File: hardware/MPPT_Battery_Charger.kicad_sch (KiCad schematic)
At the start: 76 parts, among them Q24 SI7414DN-T1-E3, Q25 SI7414DN-T1-E3, Q5 SI7414DN-T1-E3, Q6 SI7414DN-T1-E3, Q8 SI2302DDS-T1-GE3, U22 BQ24650RVAT, U26 LMV321RIYLT, U28 LMV321RIYLT, U4 INA199C1DCKR

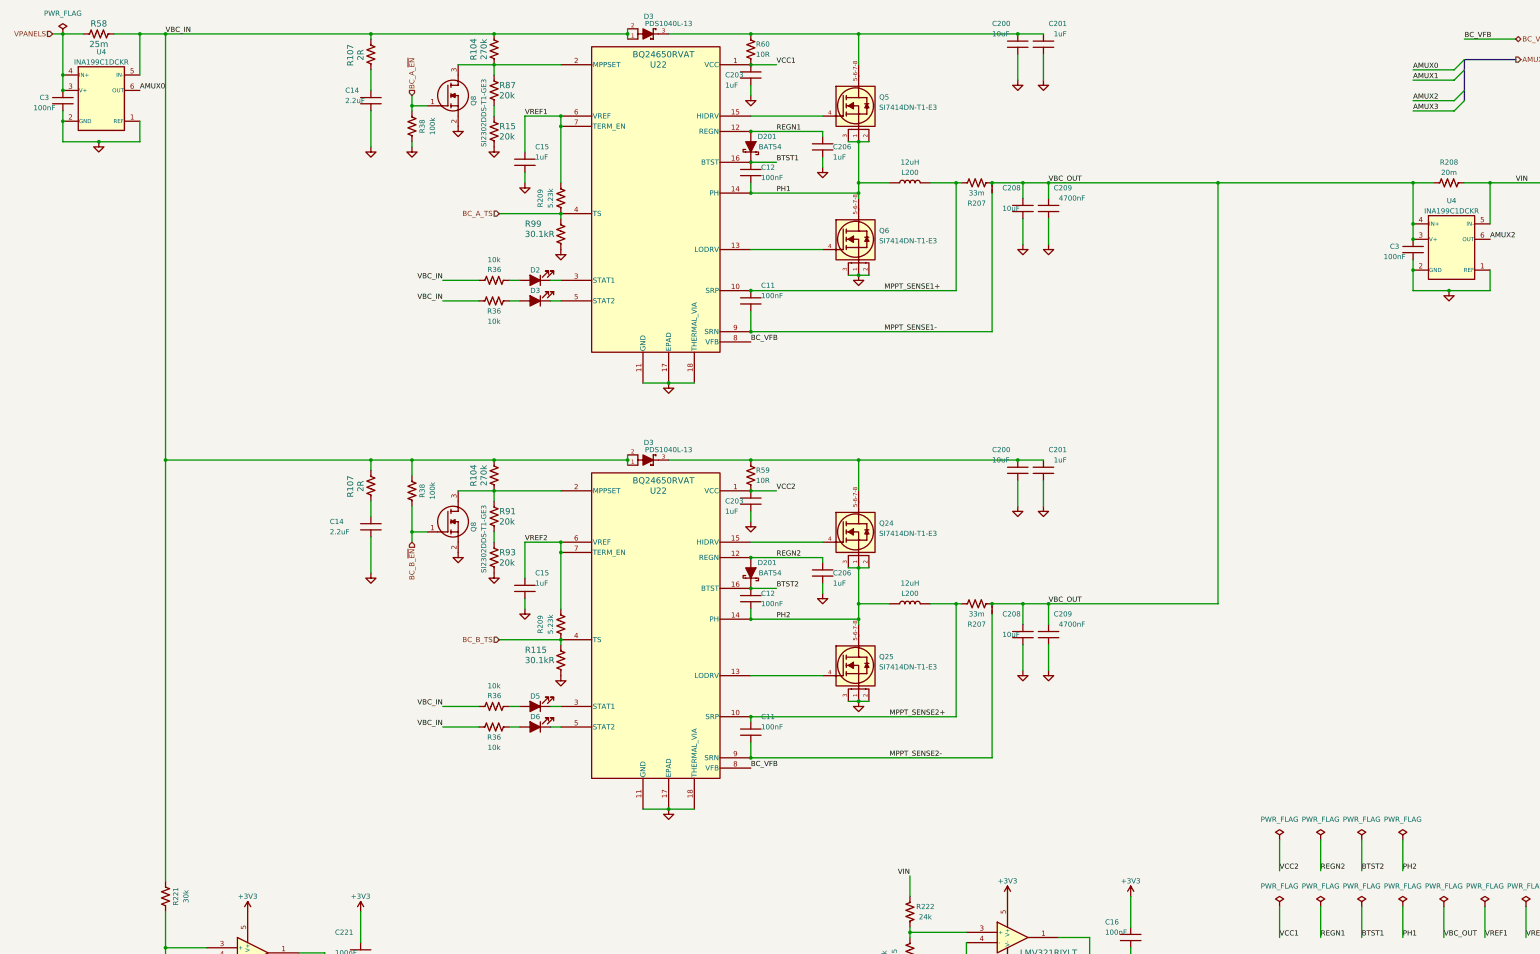
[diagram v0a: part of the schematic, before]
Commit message: hardware: Making corrections regarding #15, #14, #13 and starting #12 and #11.
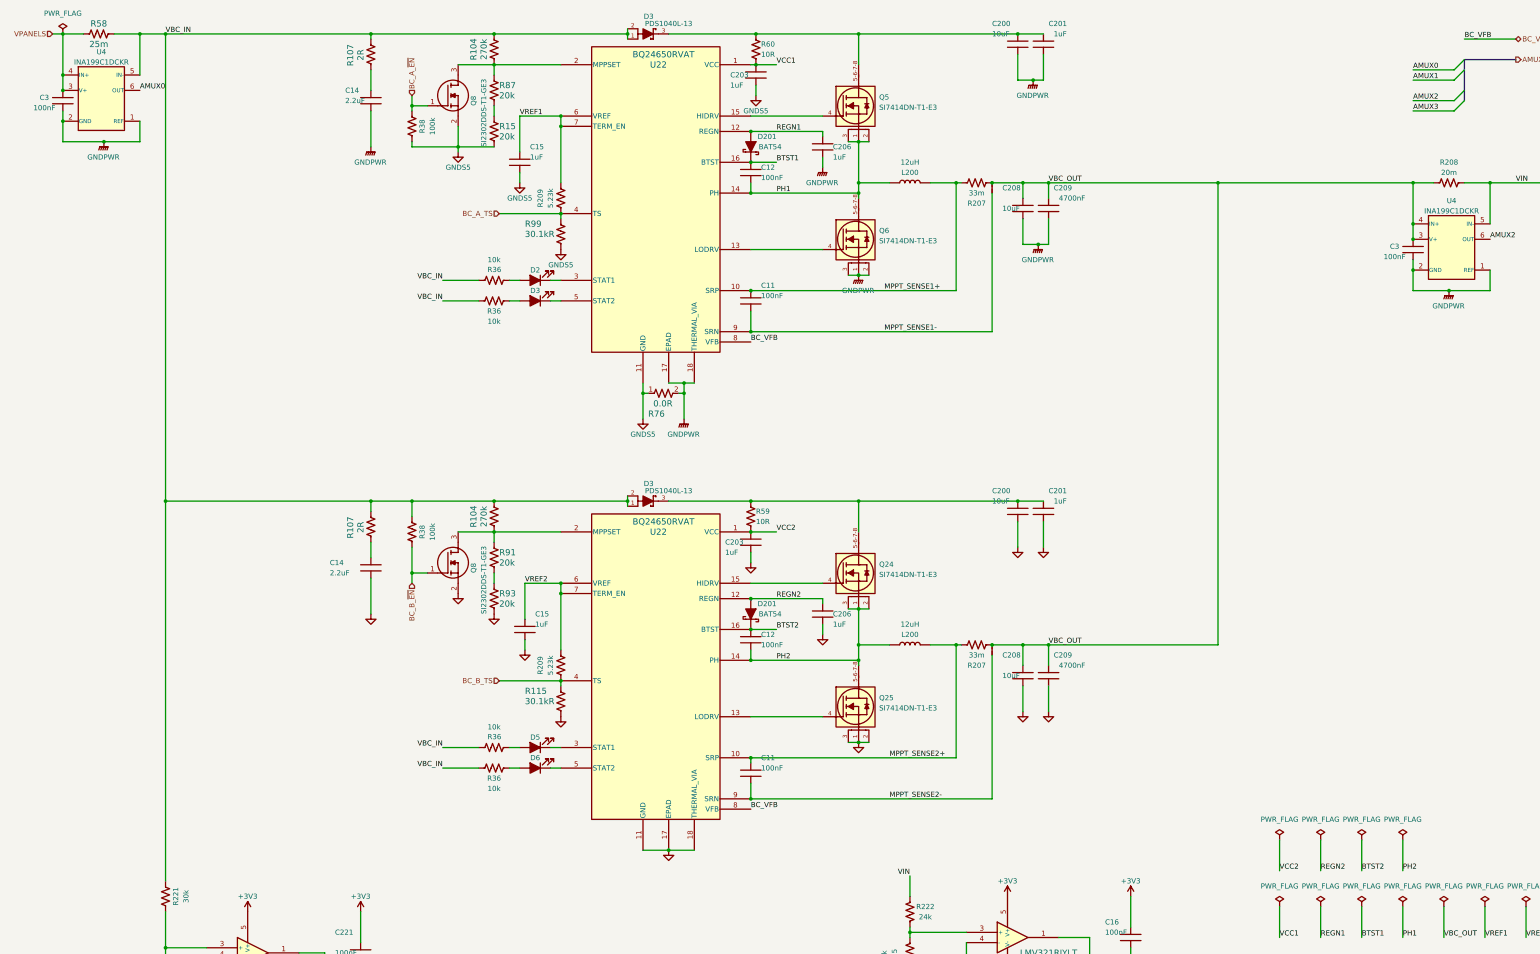
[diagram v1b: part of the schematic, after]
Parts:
- added R76: 0.0R, footprints:CRCW06030000Z0EAHP, symbol CRCW06030000Z0EAHP:CRCW06030000Z0EAHP
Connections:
- net GND: no longer C14.2, C15.2, C200.2, C201.2, C203.2, C206.2, C208.2, C209.2, C3.2, C3.2, Q6.1 (S), Q6.2 (S), Q6.3 (S), Q8.2 (S), R15.1, R38.1, R99.1, U22.11 (GND), U22.17 (EPAD), U22.18 (THERMAL_VIA), U4.1 (REF), U4.1 (REF), U4.2 (GND), U4.2 (GND)
- new net GNDPWR: C14.2, C200.2, C201.2, C206.2, C208.2, C209.2, C3.2, C3.2, Q6.1 (S), Q6.2 (S), Q6.3 (S), R76.2, U22.17 (EPAD), U22.18 (THERMAL_VIA), U4.1 (REF), U4.1 (REF), U4.2 (GND), U4.2 (GND)
- new net GNDS5: C15.2, C203.2, Q8.2 (S), R15.1, R38.1, R76.1, R99.1, U22.11 (GND)
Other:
- moved on the sheet: C11, C12, C14, C15, C200, C201, C203, C206, C208, C209, D201, D3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

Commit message: hardware: Updating the MPPT circuit.
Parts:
- removed R76: 0.0R, footprints:CRCW06030000Z0EAHP, symbol CRCW06030000Z0EAHP:CRCW06030000Z0EAHP
- JP2: symbol Jumper:Jumper -> JUMPER:JUMPER
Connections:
- net GNDPWR: now also C14.2, C16.2, C200.2, C201.2, C206.2, C208.2, C209.2, C221.2, Q25.1 (S), Q25.2 (S), Q25.3 (S), R225.2, R72.1, U22.11 (GND), U22.11 (GND), U22.18 (THERMAL_VIA), U26.2 (V-), U28.2 (V-); no longer U22.17 (EPAD)
- net GNDS5: now also U22.17 (EPAD), U22.17 (EPAD); no longer U22.11 (GND)
- removed net GND: C14.2, C15.2, C16.2, C200.2, C201.2, C203.2, C206.2, C208.2, C209.2, C221.2, Q25.1 (S), Q25.2 (S), Q25.3 (S), Q8.2 (S), R115.1, R225.2, R72.1, R93.1, U22.11 (GND), U22.17 (EPAD), U22.18 (THERMAL_VIA), U26.2 (V-), U28.2 (V-)
- new net GNDS6: C15.2, C203.2, Q8.2 (S), R115.1, R93.1
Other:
- moved on the sheet: C203, R59

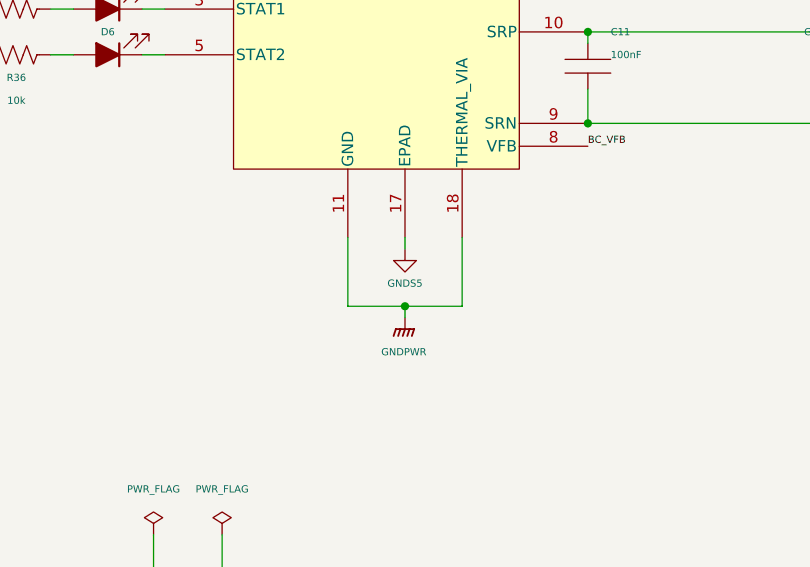
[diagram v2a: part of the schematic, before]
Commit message: hardware: First version of the RE2PS layout with all components connected.
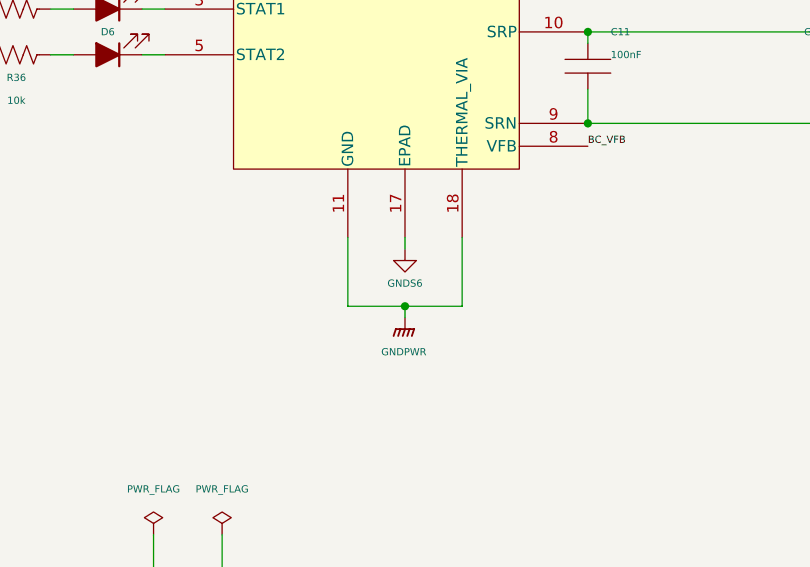
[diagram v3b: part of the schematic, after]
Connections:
- net GNDS5: no longer U22.17 (EPAD)
- net GNDS6: now also U22.17 (EPAD)
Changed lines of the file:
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@@
-    )
-  )
-  (symbol (lib_id "GNDS5:GNDS5") (at 176.53 227.33 0) (unit 1)
-    (in_bom yes) (on_board yes) (dnp no)
-    (property "Reference" "#PWR092" (at 176.53 233.68 0)
-      (effects (font (size 0.8 0.8)) hide)
-    )
-    (property "Value" "GNDS5" (at 176.53 231.14 0)
-      (effects (font (size 0.8 0.8)))
-    )
-    (property "Footprint" "" (at 176.53 227.33 0)
-      (effects (font (size 0.8 0.8)) hide)
-    )
-    (property "Datasheet" "" (at 176.53 227.33 0)
-      (effects (font (size 0.8 0.8)) hide)
-    )
-    (pin "1")
-    (instances
-      (project "eps-re_project"
-        (path "/2eebaa11-d7ed-4bfd-bc8e-988f68654d29/0b69622c-4960-45c0-904b-657ff8db02ea"
-          (reference "#PWR092") (unit 1)
-        )
-      )
     )
   )
@@
         )
       )
+    )
+  )
+  (symbol (lib_id "GNDS6:GNDS6") (at 176.53 227.33 0) (unit 1)
+    (in_bom yes) (on_board yes) (dnp no)
+    (property "Reference" "#PWR092" (at 176.53 233.68 0)
+      (effects (font (size 0.8 0.8)) hide)
+    )
+    (property "Value" "GNDS6" (at 176.53 231.14 0)
+      (effects (font (size 0.8 0.8)))
+    )
+    (property "Footprint" "" (at 176.53 227.33 0)
+      (effects (font (size 0.8 0.8)) hide)
+    )
+    (property "Datasheet" "" (at 176.53 227.33 0)
+      (effects (font (size 0.8 0.8)) hide)
+    )
+    (pin "1")
+    (instances
+      (project "eps-re_project"
+        (path "/2eebaa11-d7ed-4bfd-bc8e-988f68654d29/0b69622c-4960-45c0-904b-657ff8db02ea"
+          (reference "#PWR092") (unit 1)
+        )
+      )

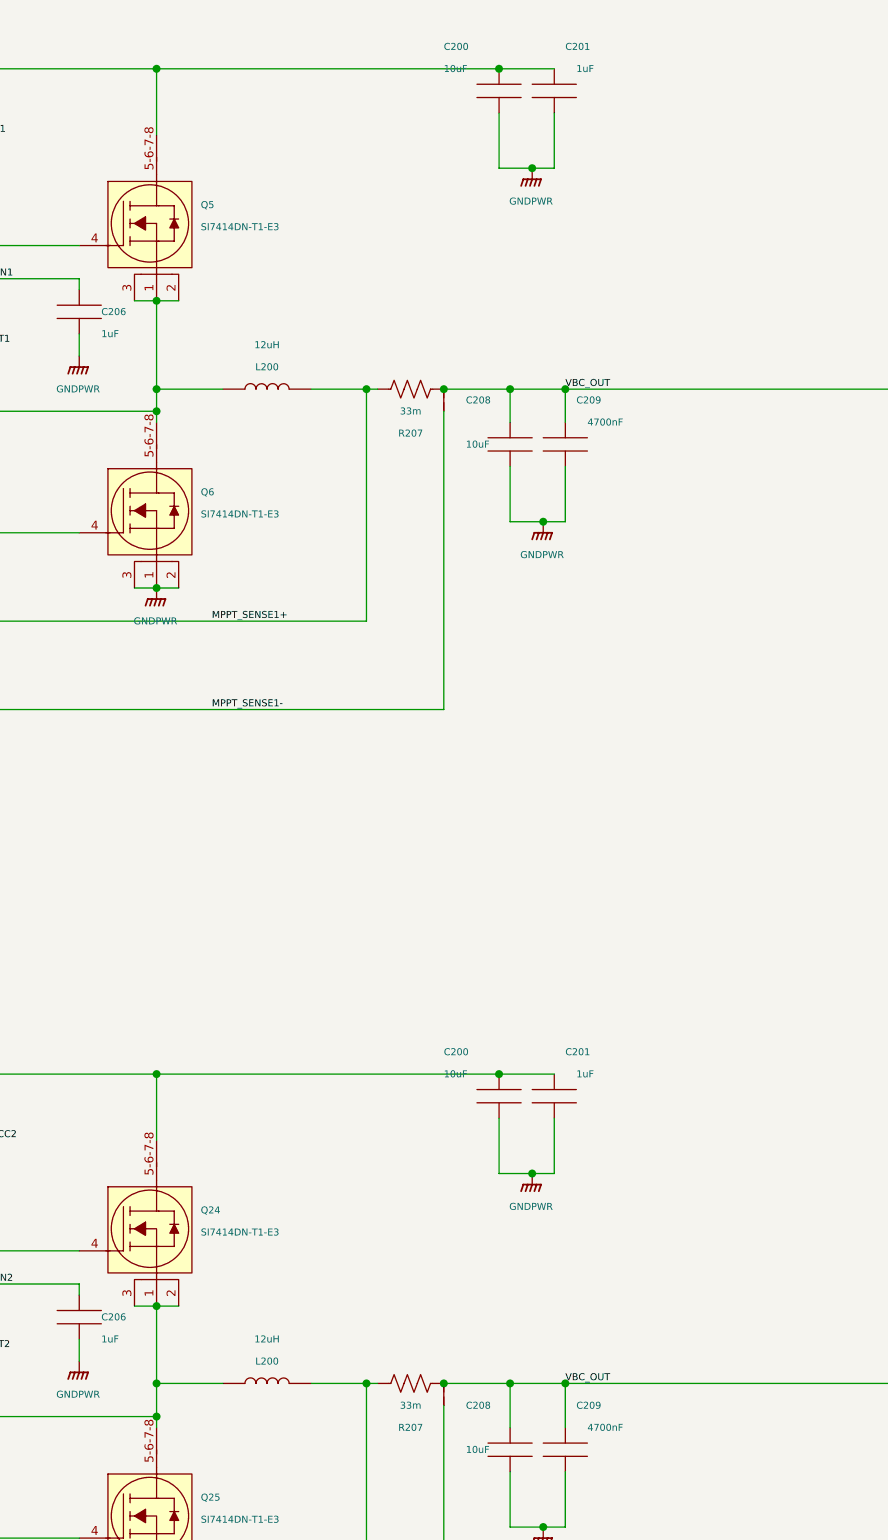
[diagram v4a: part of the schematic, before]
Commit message: hardware: Adding blocking diodes. Pass through diodes were also added in MPPT-based converters. Also, test points were added.
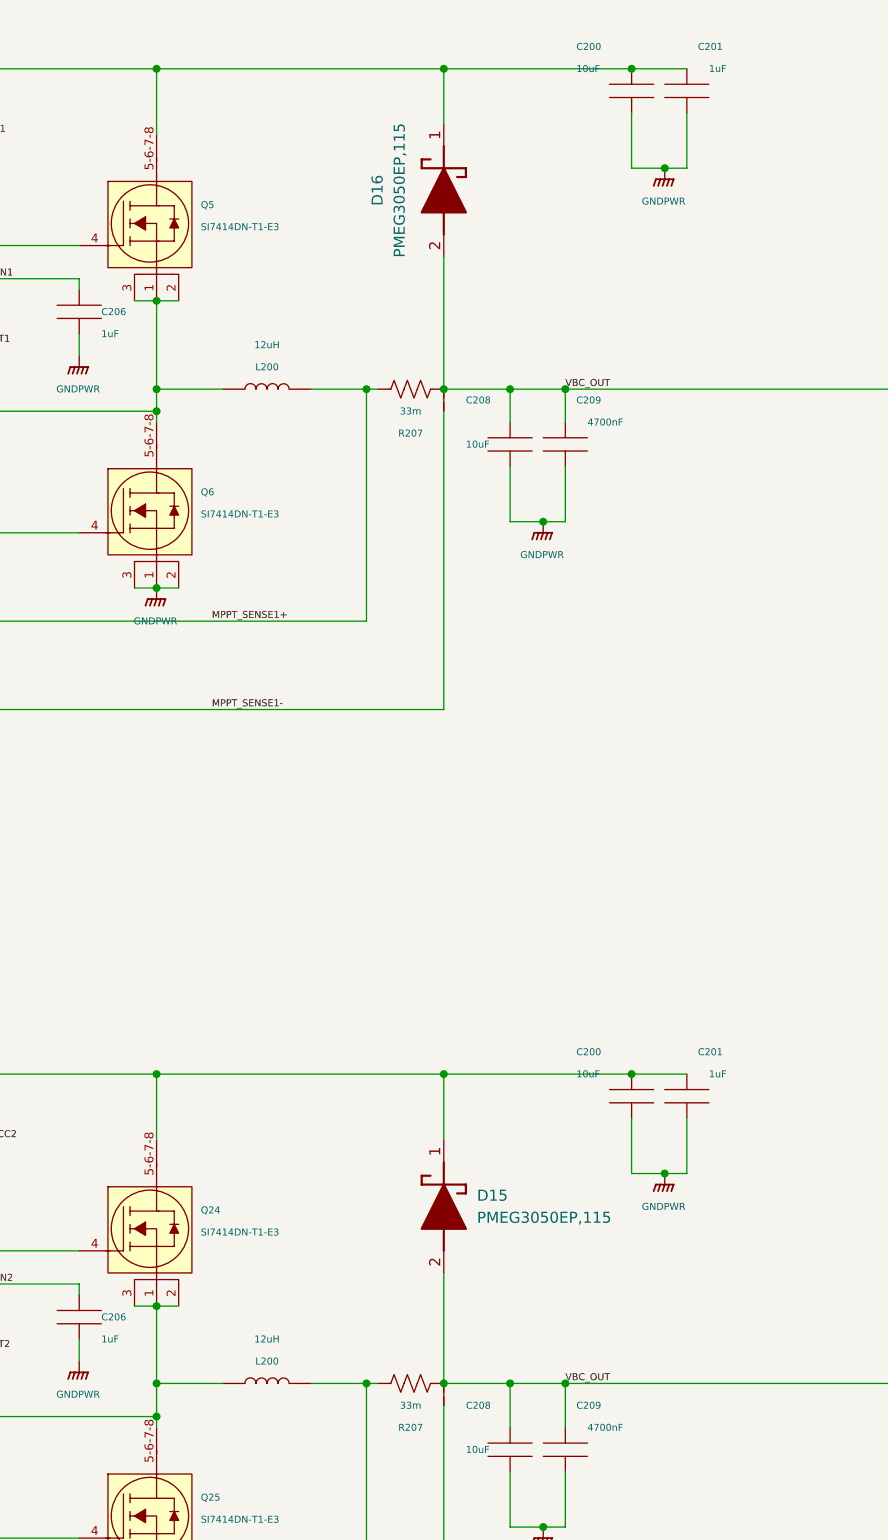
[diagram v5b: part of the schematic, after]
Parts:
- added D15, D16: PMEG3050EP,115, footprints:PMEG3050EP,115, symbol PMEG3050EP,115:PMEG3050EP,115
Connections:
- net VBC_OUT: now also D15.2 (A), D16.2 (A)
- net at C200.1, C201.1, D3.3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: now also D15.1 (K)
- net at C200.1, C201.1, D3.3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: now also D16.1 (K)
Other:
- moved on the sheet: C200, C201
